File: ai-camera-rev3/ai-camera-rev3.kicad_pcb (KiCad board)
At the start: 4 copper layers, 70 x 70 mm, 178 parts, among them J1 Conn-01x02_P2mm_NONAME_JST-PH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, J2 TYPE-C-31-M-12, J3 MAXLAB, J4 Conn-02x10_P2.54mm_B-2100S20P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, J5 Conn-01x02_P1.25mm_10114829-1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, J6 Conn_01x24_FFC_0.5mm_AFC01-S2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, Q1 2N7002, Q10 2N7002, Q2 2N7002, Q3 AO3401A, Q4 AO3401A, Q5 2N7002, Q6 AO3401A, Q7 2N7002, Q8 AO3401A, Q9 2N7002, SW1 SW_PB_90deg_K2-1102AQ-H4CW-01, SW2 SW_PB_TS-1187A-B-A-B, SW3 SW_PB_TS-1187A-B-A-B, SW4 SW_PB_90deg_K2-1102AQ-H4CW-01, U1 TP4057-42-SOT26-R, U10 ESP32-S3-WROOM-1-N16R8, U11 MT9284-28J, U12 LTR-303ALS-01, U2 XC6206-2.8V, U3 PCF85063AT_SO8, U4 SOT-23-6_SN74LVC1G373DBVR_TI, U5 SY8089AAAC, U6 PIR_AS312, U7 XC6206-2.8V, U8 RT9166-12GVL, U9 AP1511B, Y1 32.768kHz_Q13FC1350000400

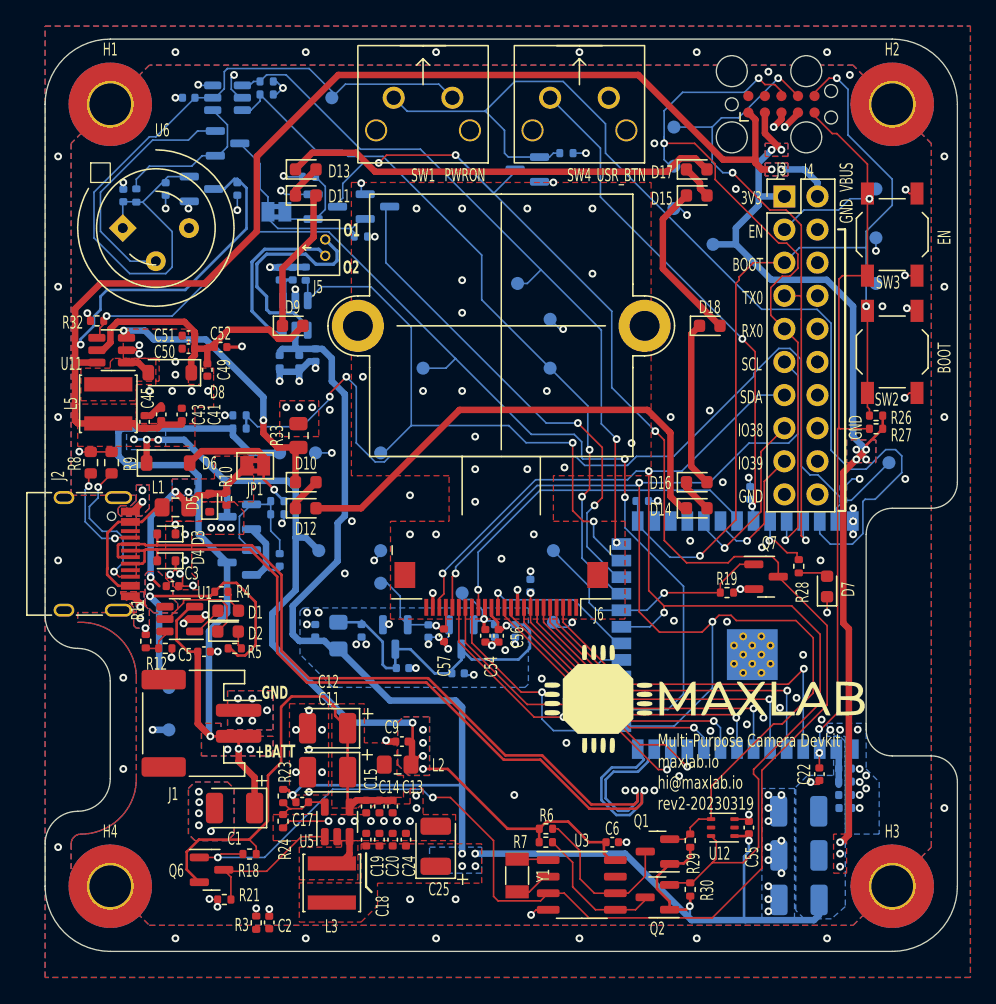
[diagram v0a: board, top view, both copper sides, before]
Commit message: EAC-60: rev3: fix all errors and warnings from 7.0.2 KiCAD, update to newer KIML
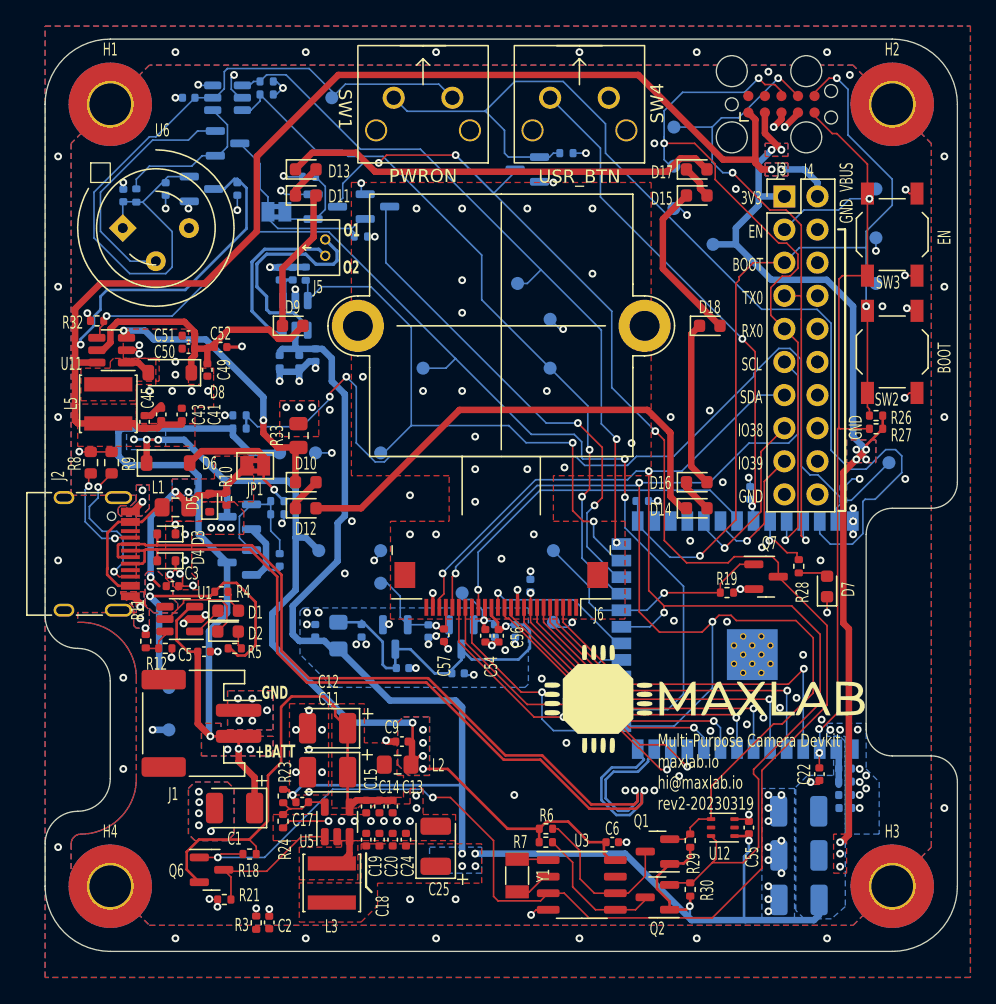
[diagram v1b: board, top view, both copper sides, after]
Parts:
- SW1, SW4: footprint 00-kiml-button-switch-tht:SW_PB_90deg_K2-1102AQ-H4CW-01 -> 00-kiml-switch-button-tht:SW_PB_90deg_K2-1102AQ-H4CW-01
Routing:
- net +1V2: track 5.17 -> 6.10 mm

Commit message: EAC-60: rev3: use proper buttons and update KIML reference
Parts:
- L1, L2, L4: value 0805_FB_220R@100MHz_BLM21PG221SN1D -> FB_2A_0805_220R@100MHz_BLM21PG221SN1D
- L3, L5: value 10u_SWPA4030S100MT -> 10u_1.5A_4x4mm_SWPA4030S100MT
- U3: value PCF85063AT_SO8 -> PCF85063AT
- U4: value SOT-23-6_SN74LVC1G373DBVR_TI -> TI_SN74LVC1G373DBVR
